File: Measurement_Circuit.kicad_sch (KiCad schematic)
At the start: 1 part, among them U1 ADE7953xCP

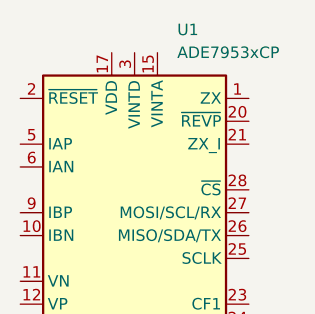
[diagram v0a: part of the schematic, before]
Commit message: Microcontroller draft
Created a draft of the things connected to the microcontroller.
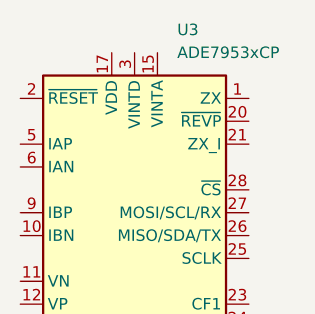
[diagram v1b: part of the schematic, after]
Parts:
- renumbered U1 to U3
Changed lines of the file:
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@@
   (symbol (lib_id "Sensor:ADE7953xCP") (at 135.89 74.93 0) (unit 1)
     (in_bom yes) (on_board yes) (dnp no) (fields_autoplaced)
-    (property "Reference" "U1" (at 140.6241 46.99 0)
+    (property "Reference" "U3" (at 140.6241 46.99 0)
       (effects (font (size 1.27 1.27)) (justify left))
     )
@@
       (project "Eng_Thesis"
         (path "/97bd1b5a-123d-47f8-a974-72569e0e2197/169631cb-4600-41da-8cbe-8c1369144896"
-          (reference "U1") (unit 1)
+          (reference "U3") (unit 1)
         )
       )

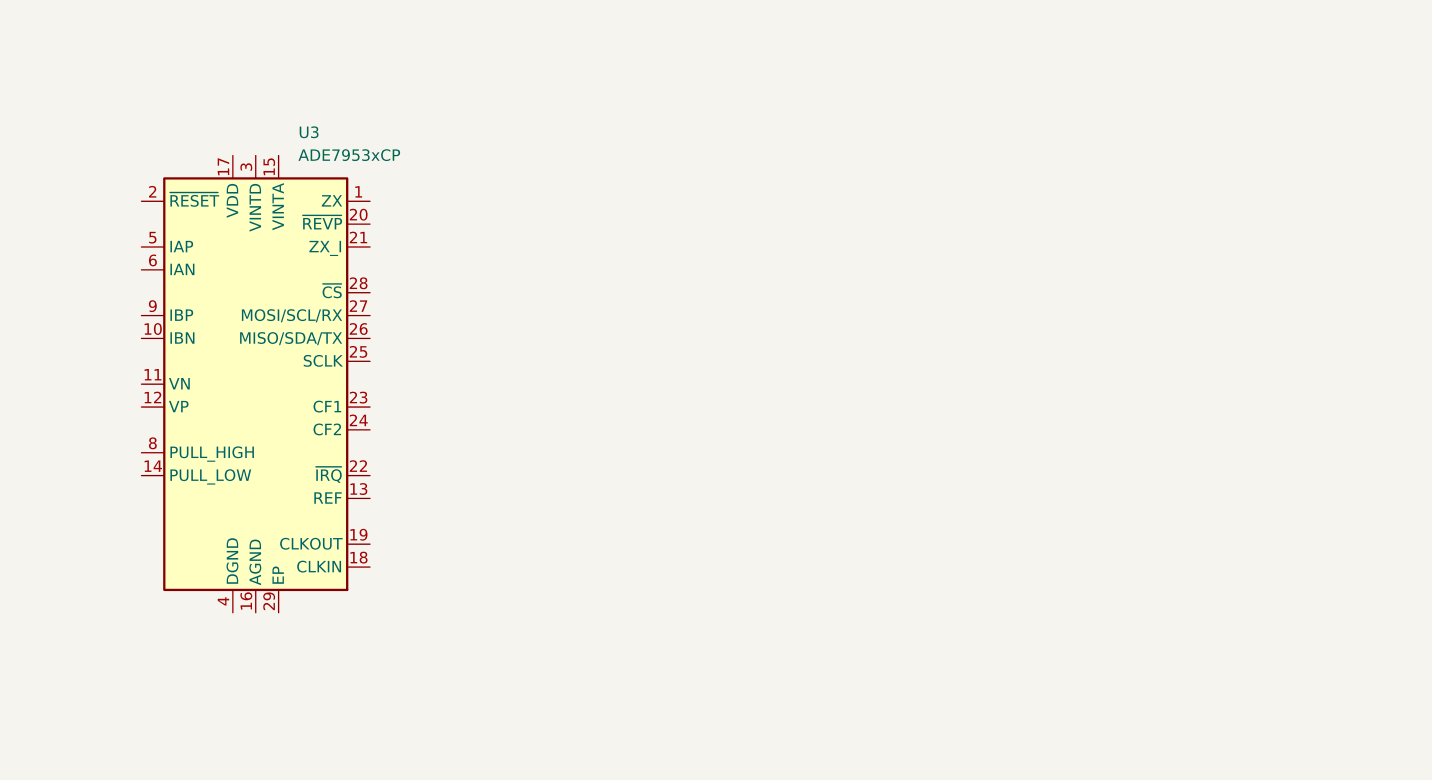
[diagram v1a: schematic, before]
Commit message: Partial measurement block
Added capacitor in Power, fixed the debug junction, added initial draft of measurement block
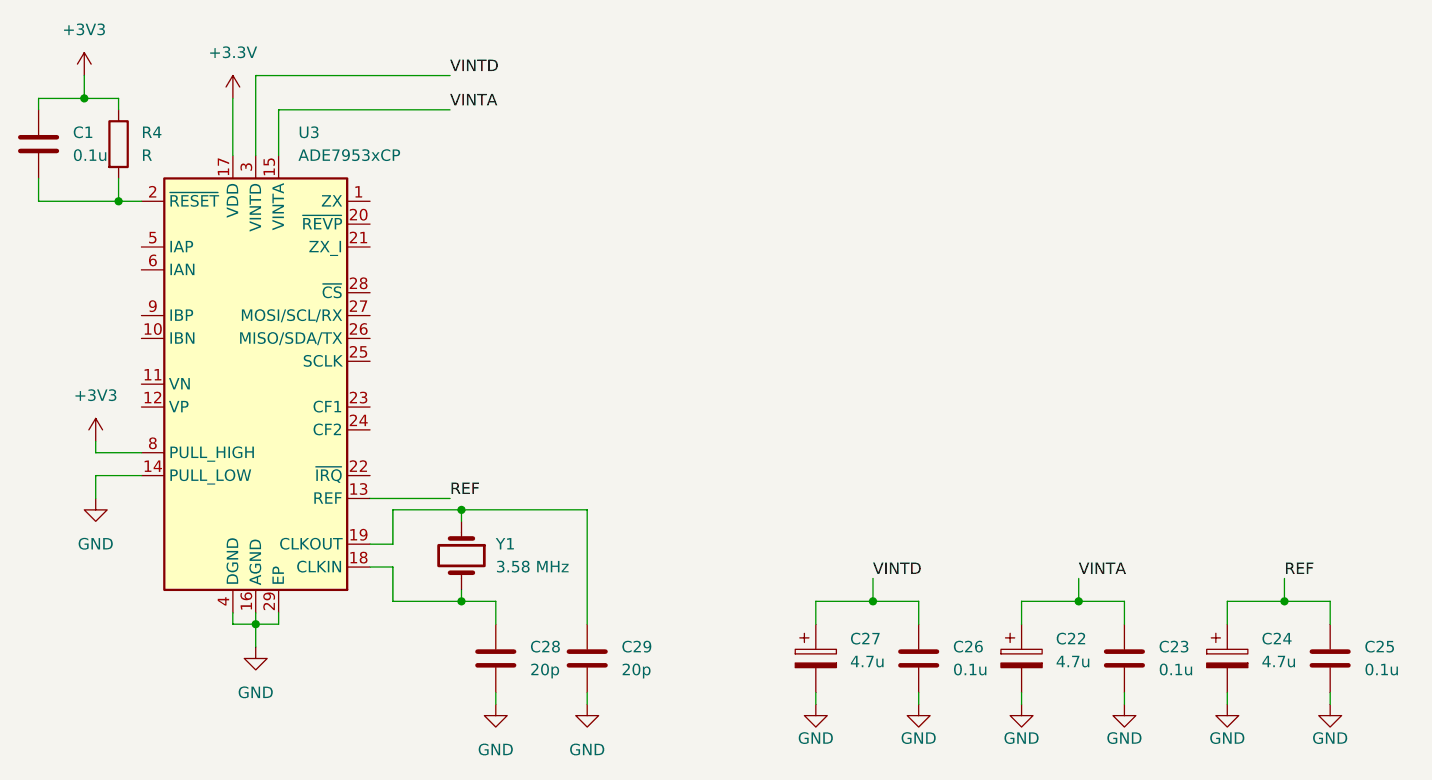
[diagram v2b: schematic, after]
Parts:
- added C1, C23, C25, C26: 0.1u, symbol Device:C
- added C22, C24, C27: 4.7u, symbol Device:C_Polarized
- added C28, C29: 20p, symbol Device:C
- added R4: R, symbol Device:R
- added Y1: 3.58 MHz, symbol Device:Crystal
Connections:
- net REF: now reaches U3.13 (REF)
- net REF: now also C24.1, C25.1
- net GND: now reaches U3.14 (PULL_LOW)
- net GND: now also U3.16 (AGND), U3.29 (EP), U3.4 (DGND), C22.2, C23.2, C24.2, C25.2, C26.2, C27.2, C28.2, C29.2
- net VINTA: now reaches U3.15 (VINTA)
- net VINTA: now also C22.1, C23.1
- net +3.3V: now reaches U3.17 (VDD)
- net at U3.18 (CLKIN): now also C28.1, Y1.2
- net at U3.19 (CLKOUT): now also C29.1, Y1.1
- net at U3.2 (~{RESET}): now also C1.2, R4.2
- net VINTD: now reaches U3.3 (VINTD)
- net VINTD: now also C26.1, C27.1
- net +3V3: now reaches U3.7 (PULL_HIGH), U3.8 (PULL_HIGH)
- net +3V3: now also C1.1, R4.1

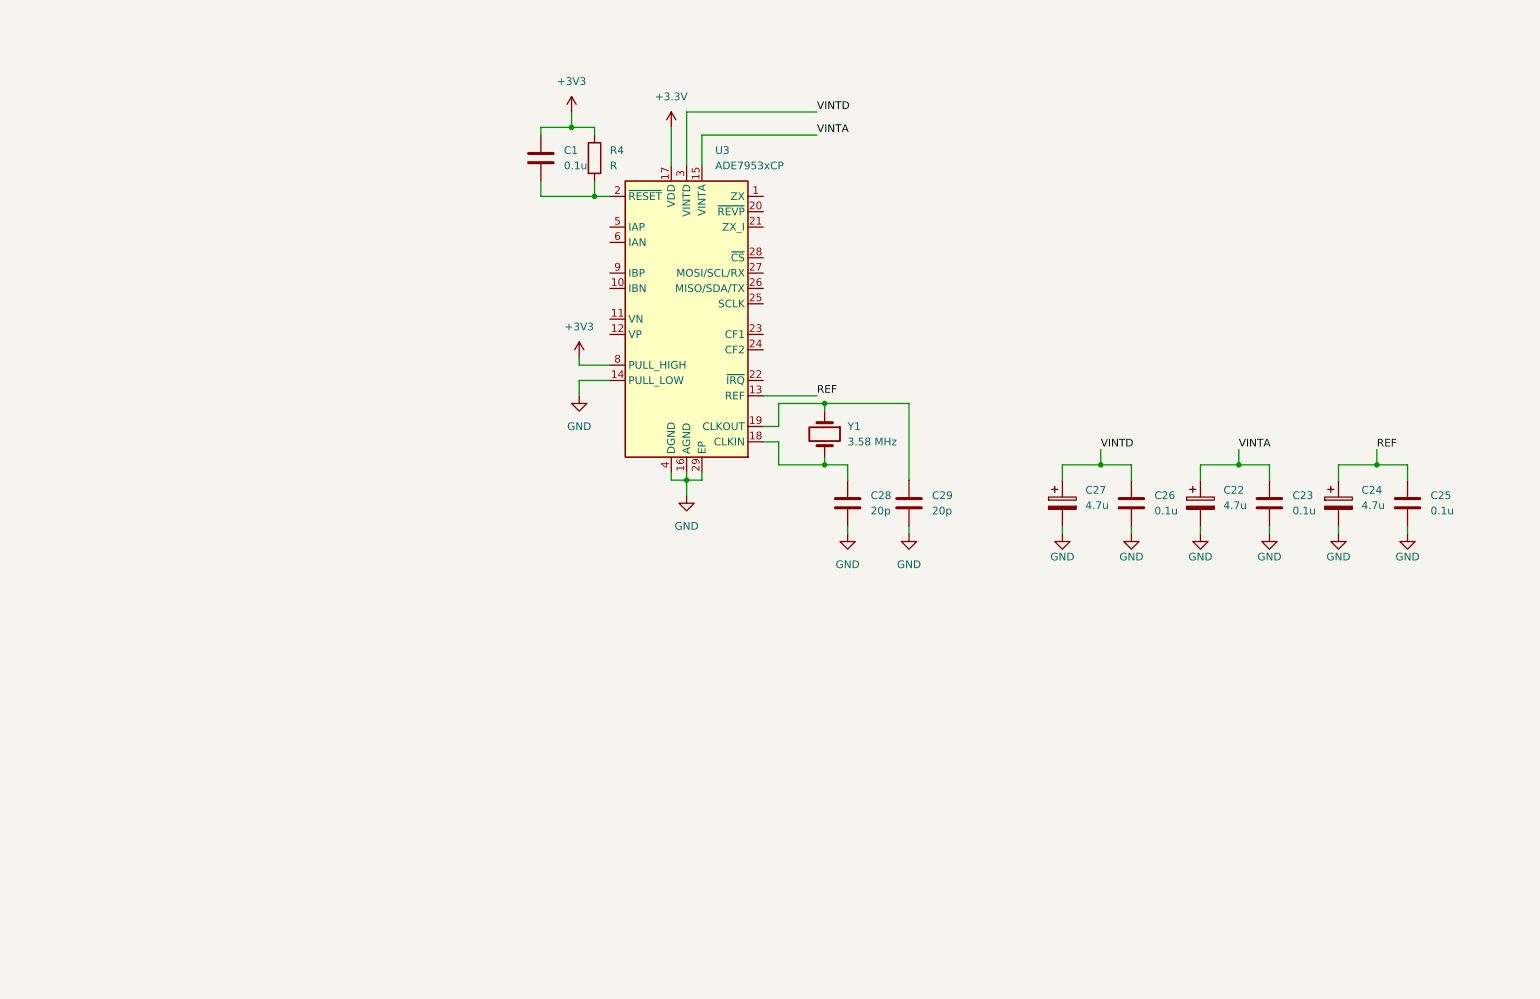
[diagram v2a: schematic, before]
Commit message: Progress in measurement + rework of power
Progressed in measurement circuit, and reworked the power supply to be isolated
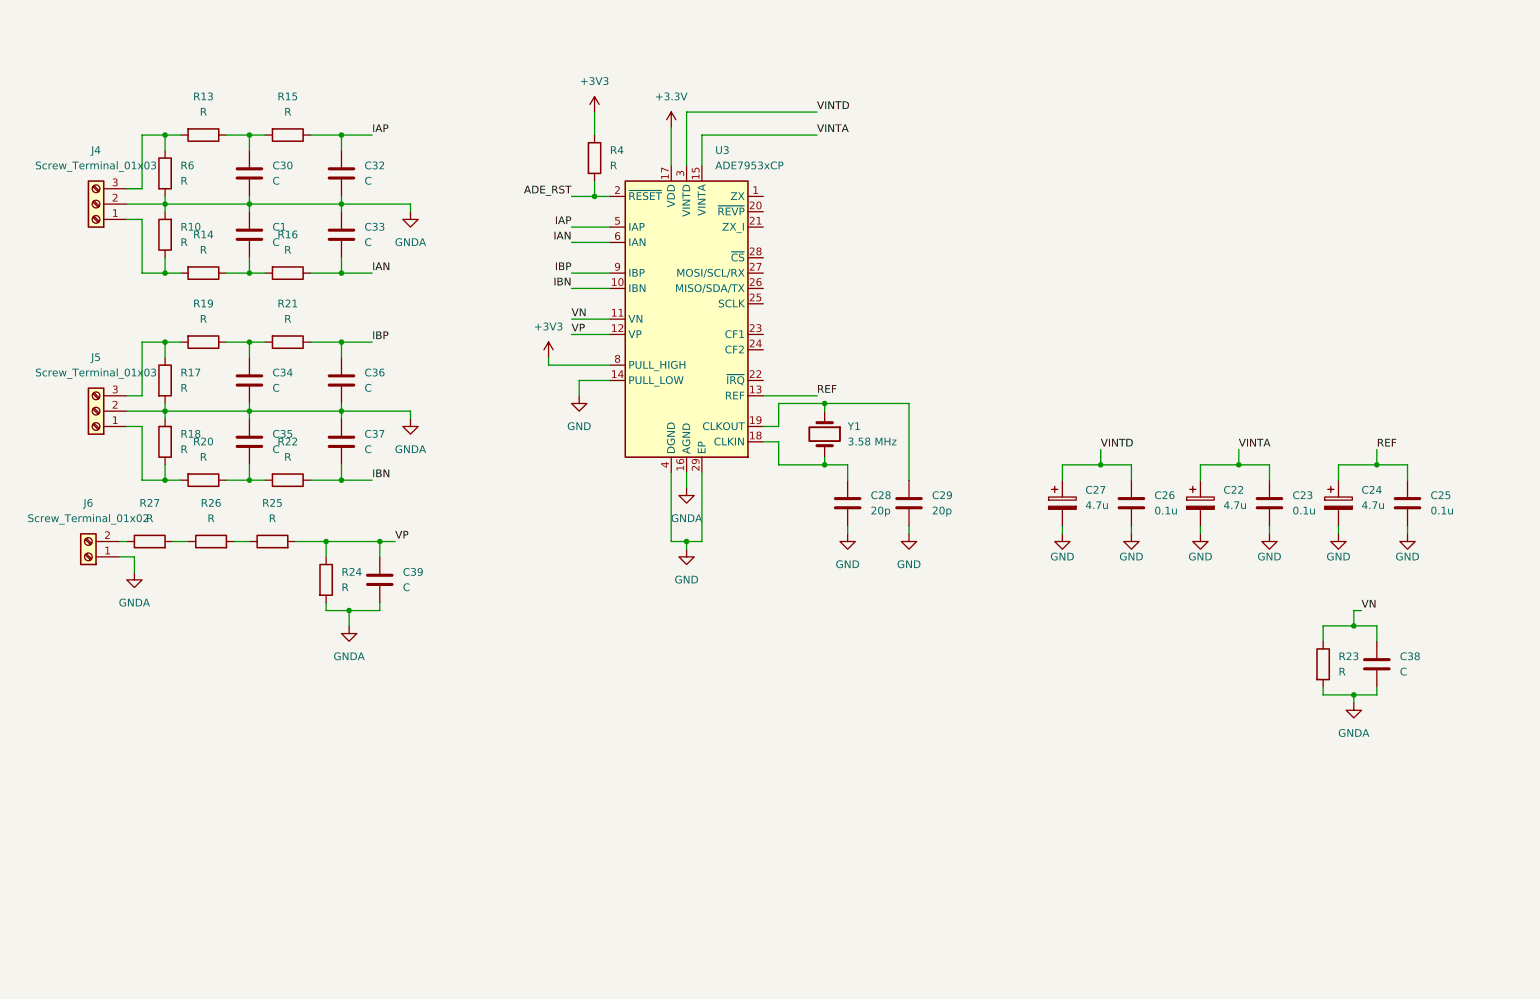
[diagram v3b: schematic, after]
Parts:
- added C30, C32, C33, C34, C35, C36, C37, C38, C39: C, symbol Device:C
- added J4, J5: Screw_Terminal_01x03, symbol Connector:Screw_Terminal_01x03
- added J6: Screw_Terminal_01x02, symbol Connector:Screw_Terminal_01x02
- added R10, R13, R14, R15, R16, R17, R18, R19, R20, R21, R22, R23, R24, R25, R26, R27, R6: R, symbol Device:R
- C1: value 0.1u -> C
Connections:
- net +3V3: no longer C1.1
- net GND: no longer U3.16 (AGND)
- net ADE_RST: now reaches R4.2, U3.2 (~{RESET})
- net ADE_RST: no longer C1.2
- net IBN: now reaches U3.10 (IBN)
- net IBN: now also C37.2, R22.1
- net VN: now reaches U3.11 (VN)
- net VN: now also C38.1, R23.1
- net VP: now reaches U3.12 (VP)
- net VP: now also C39.1, R24.1, R25.2
- net IAP: now reaches U3.5 (IAP)
- net IAP: now also C32.1, R15.1
- net IAN: now reaches U3.6 (IAN)
- net IAN: now also C33.2, R16.1
- net IBP: now reaches U3.9 (IBP)
- net IBP: now also C36.1, R21.1
- new net: C35.2, R20.1, R22.2
- new net: C30.1, R13.1, R15.2
- new net: J6.2 (Pin_2), R27.1
- new net: J5.3 (Pin_3), R17.1, R19.2
- new net: R25.1, R26.2
- new net: J5.1 (Pin_1), R18.1, R20.2
- new net: R26.1, R27.2
- new net: C34.1, R19.1, R21.2
- new net: J4.1 (Pin_1), R10.1, R14.2
- new net: J4.3 (Pin_3), R13.2, R6.1
- new net: C1.2, R14.1, R16.2
- new net GNDA: C1.1, C30.2, C32.2, C33.1, C34.2, C35.1, C36.2, C37.1, C38.2, C39.2, J4.2 (Pin_2), J5.2 (Pin_2), J6.1 (Pin_1), R10.2, R17.2, R18.2, R23.2, R24.2, R6.2, U3.16 (AGND)

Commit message: Filter values + isolation draft
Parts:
- added IC1: ISO6721RBDR, SOIC127P600X175-8N, symbol LibLoader:ISO6721RBDR
- added R30, R31: R, symbol Device:R
- added U8: ISO1541, Package_SO:SOIC-8_3.9x4.9mm_P1.27mm, symbol Isolator:ISO1541
- C1, C30, C32, C33, C34, C35, C36, C37, C38, C39: value C -> 33n
- R10, R17, R18, R6: value R -> 51
- R13, R14, R19, R20: value R -> 100
- R15, R16, R21, R22, R23, R24: value R -> 1k
- R25, R26: value R -> 100k
- R27: value R -> 55k
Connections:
- net +3V3: now also R30.1, R31.1
- net ADE_RST: now also IC1.3 (OUTB)
- net ADE_IRQ: now reaches U3.22 (~{IRQ})
- net ADE_IRQ: now also IC1.2 (INA)
- net at U3.25 (SCLK): now also R31.2
- net ADE_SDA: now reaches U3.26 (MISO/SDA/TX)
- net ADE_SDA: now also U8.6 (SCL2)
- net ADE_SCL: now reaches U3.27 (MOSI/SCL/RX)
- net ADE_SCL: now also U8.7 (SDA2)
- net at U3.28 (~{CS}): now also R30.2
- new net I2C2_SCL: U8.2 (SDA1)
- new net I2C2_SDA: U8.3 (SCL1)
- new net STM_ADE_IRQ: IC1.7 (OUTA)
- new net STM_ADE_RST: IC1.6 (INB)
- no-connect marks 0 -> 5
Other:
- moved on the sheet: C39, J6, R24, R25, R26, R27
